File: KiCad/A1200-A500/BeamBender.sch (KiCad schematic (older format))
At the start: 67 parts, among them J1 4-1734742-0, J2 HDMI_A_1.4, J3 STX-3501-3N, J4 Phoenix_Contact, J5 Conn_01x01, U1 LM1117-3.3, U3 ADV7513BSWZ, U4 MCP1702T-1802E_CB, X1 Abracon ASE-27.000MHZ-L-R-T, X2 Oscillator_7.0x5.0mm

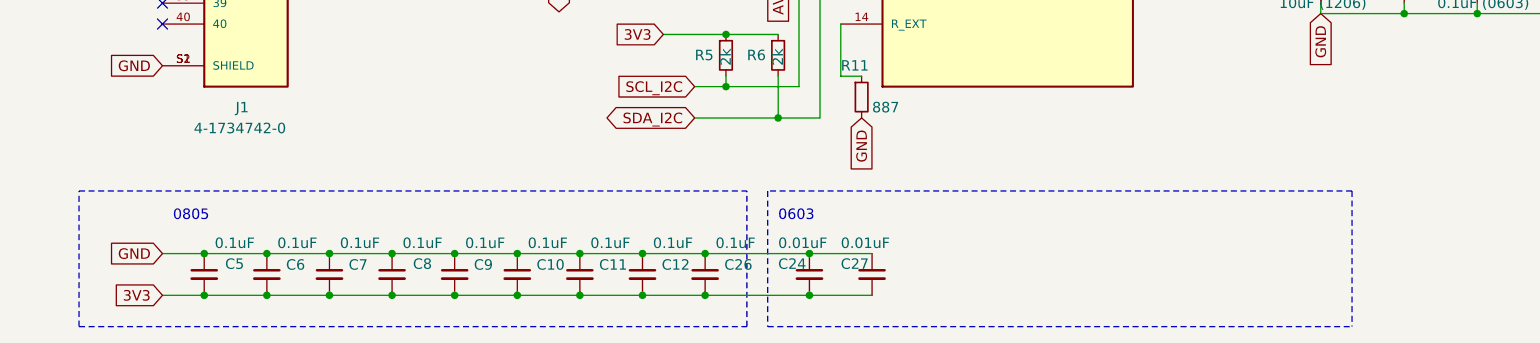
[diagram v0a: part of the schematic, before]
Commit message: Fixed JTAG-connector and remaining 3V3-power routing and pull-ups for FPGA
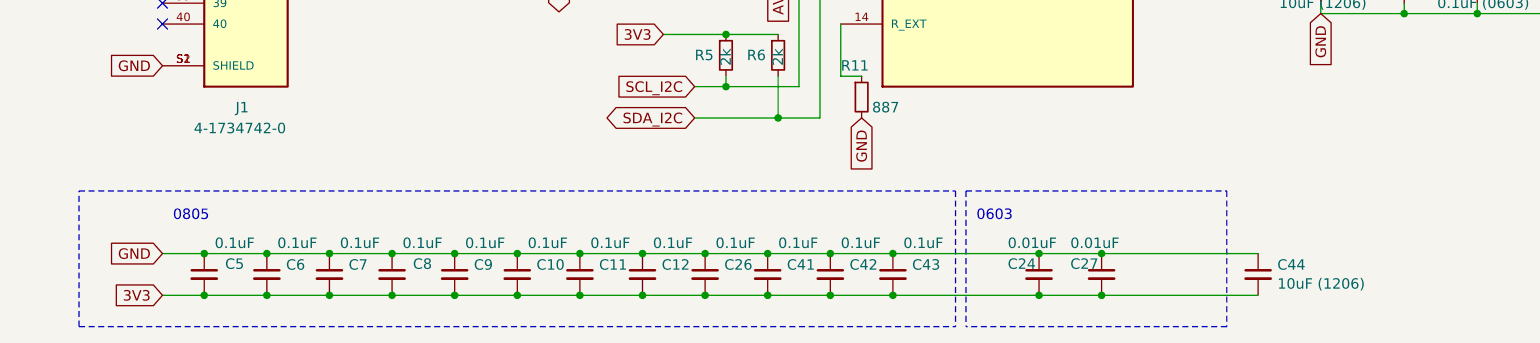
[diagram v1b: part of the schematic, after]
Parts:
- added C41, C42, C43: 0.1uF, Capacitor_SMD:C_0805_2012Metric_Pad1.18x1.45mm_HandSolder, symbol Device:C_Small
- added C44: 10uF (1206), Capacitor_SMD:C_1206_3216Metric_Pad1.33x1.80mm_HandSolder, symbol Device:C_Small
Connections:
- net 3V3: now also C41.2, C42.2, C43.2, C44.2
- net GND: now also C41.1, C42.1, C43.1, C44.1
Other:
- moved on the sheet: C24, C27
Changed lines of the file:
@@
 Connection ~ 2250 7400
 Connection ~ 2250 7600
-Wire Notes Line
-	6850 7100 6850 7750
-Text Notes 4100 7250 0    50   ~ 0
+Text Notes 5050 7250 0    50   ~ 0
 0603
 Wire Wire Line
@@
 L Device:C_Small C24
 U 1 1 6584F5FE
-P 4250 7500
-F 0 "C24" H 4100 7550 50  0000 L CNN
-F 1 "0.01uF" H 4100 7650 50  0000 L CNN
-F 2 "Capacitor_SMD:C_0603_1608Metric_Pad1.08x0.95mm_HandSolder" H 4250 7500 50  0001 C CNN
-F 3 "~" H 4250 7500 50  0001 C CNN
-	1    4250 7500
+P 5350 7500
+F 0 "C24" H 5200 7550 50  0000 L CNN
+F 1 "0.01uF" H 5200 7650 50  0000 L CNN
+F 2 "Capacitor_SMD:C_0603_1608Metric_Pad1.08x0.95mm_HandSolder" H 5350 7500 50  0001 C CNN
+F 3 "~" H 5350 7500 50  0001 C CNN
+	1    5350 7500
 	1    0    0    -1
 $EndComp
@@
 Connection ~ 3450 7400
 Connection ~ 3450 7600
-Wire Notes Line
-	3950 7750 3950 7100
-Wire Notes Line
-	750  7100 3950 7100
-Wire Notes Line
-	750  7750 3950 7750
 Wire Wire Line
 	3450 7400 3750 7400
 Wire Wire Line
 	3450 7600 3750 7600
-Wire Notes Line
-	4050 7100 4050 7750
-Wire Notes Line
-	4050 7750 6850 7750
-Wire Notes Line
-	6850 7100 4050 7100
 $Comp
 L Device:C_Small C26
@@
 $EndComp
 Connection ~ 3750 7400
-Wire Wire Line
-	3750 7400 4250 7400
 Connection ~ 3750 7600
-Wire Wire Line
-	3750 7600 4250 7600
 $Comp
 L Device:C_Small C27
 U 1 1 659B84AB
-P 4550 7500
-F 0 "C27" H 4400 7550 50  0000 L CNN
-F 1 "0.01uF" H 4400 7650 50  0000 L CNN
-F 2 "Capacitor_SMD:C_0603_1608Metric_Pad1.08x0.95mm_HandSolder" H 4550 7500 50  0001 C CNN
-F 3 "~" H 4550 7500 50  0001 C CNN
-	1    4550 7500
-	1    0    0    -1
-$EndComp
-Wire Wire Line
-	4250 7400 4550 7400
-Connection ~ 4250 7400
-Wire Wire Line
-	4250 7600 4550 7600
-Connection ~ 4250 7600
+P 5650 7500
+F 0 "C27" H 5500 7550 50  0000 L CNN
+F 1 "0.01uF" H 5500 7650 50  0000 L CNN
+F 2 "Capacitor_SMD:C_0603_1608Metric_Pad1.08x0.95mm_HandSolder" H 5650 7500 50  0001 C CNN
+F 3 "~" H 5650 7500 50  0001 C CNN
+	1    5650 7500
+	1    0    0    -1
+$EndComp
 $Comp
 L BeamBender:MCP1702T-1802E_CB U4
@@
 Text Notes 6100 3850 0    50   ~ 0
 Drill-hole guide\nfor A500 \n12.5 mm drill
+Wire Wire Line
+	3750 7400 4050 7400
+Wire Wire Line
+	3750 7600 4050 7600
+$Comp
+L Device:C_Small C41
+U 1 1 6639D585
+P 4050 7500
+F 0 "C41" H 4142 7546 50  0000 L CNN
+F 1 "0.1uF" H 4100 7650 50  0000 L CNN
+F 2 "Capacitor_SMD:C_0805_2012Metric_Pad1.18x1.45mm_HandSolder" H 4050 7500 50  0001 C CNN
+F 3 "~" H 4050 7500 50  0001 C CNN
+	1    4050 7500
+	1    0    0    -1
+$EndComp
+Connection ~ 4050 7400
+Wire Wire Line
+	4050 7400 4350 7400
+Connection ~ 4050 7600
+Wire Wire Line
+	4050 7600 4350 7600
+$Comp
+L Device:C_Small C42
+U 1 1 6639DFDF
+P 4350 7500
+F 0 "C42" H 4442 7546 50  0000 L CNN
+F 1 "0.1uF" H 4400 7650 50  0000 L CNN
+F 2 "Capacitor_SMD:C_0805_2012Metric_Pad1.18x1.45mm_HandSolder" H 4350 7500 50  0001 C CNN
+F 3 "~" H 4350 7500 50  0001 C CNN
+	1    4350 7500
+	1    0    0    -1
+$EndComp
+Connection ~ 4350 7400
+Connection ~ 4350 7600
+$Comp
+L Device:C_Small C43
+U 1 1 6639EB03
+P 4650 7500
+F 0 "C43" H 4742 7546 50  0000 L CNN
+F 1 "0.1uF" H 4700 7650 50  0000 L CNN
+F 2 "Capacitor_SMD:C_0805_2012Metric_Pad1.18x1.45mm_HandSolder" H 4650 7500 50  0001 C CNN
+F 3 "~" H 4650 7500 50  0001 C CNN
+	1    4650 7500
+	1    0    0    -1
+$EndComp
+Wire Wire Line
+	4350 7400 4650 7400
+Wire Wire Line
+	4350 7600 4650 7600
+Wire Notes Line
+	5000 7100 5000 7750
+Wire Wire Line
+	4650 7400 5350 7400
+Connection ~ 4650 7400
+Connection ~ 5350 7400
+Wire Wire Line
+	5350 7400 5650 7400
+Wire Wire Line
+	4650 7600 5350 7600
+Connection ~ 4650 7600
+Connection ~ 5350 7600
+Wire Wire Line
+	5350 7600 5650 7600
+Wire Notes Line
+	4950 7100 4950 7750
+Wire Notes Line
+	750  7100 4950 7100
+Wire Notes Line
+	750  7750 4950 7750
+$Comp
+L Device:C_Small C44
+U 1 1 66443446
+P 6400 7500
+F 0 "C44" H 6492 7546 50  0000 L CNN
+F 1 "10uF (1206)" H 6492 7455 50  0000 L CNN
+F 2 "Capacitor_SMD:C_1206_3216Metric_Pad1.33x1.80mm_HandSolder" H 6400 7500 50  0001 C CNN
+F 3 "~" H 6400 7500 50  0001 C CNN
+	1    6400 7500
+	1    0    0    -1
+$EndComp
+Wire Notes Line
+	5000 7100 6250 7100
+Wire Notes Line
+	6250 7100 6250 7750
+Wire Notes Line
+	6250 7750 5000 7750
+Wire Wire Line
+	5650 7400 6400 7400
+Connection ~ 5650 7400
+Wire Wire Line
+	5650 7600 6400 7600
+Connection ~ 5650 7600
 $EndSCHEMATC

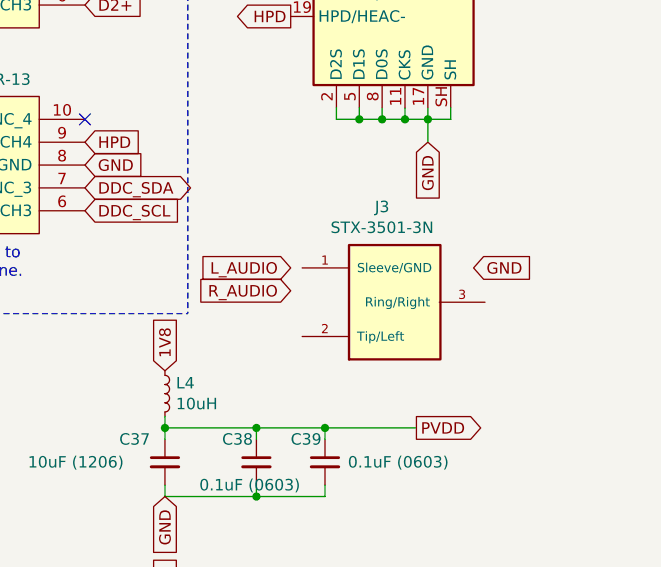
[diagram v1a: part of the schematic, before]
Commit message: assigned the audio Left and Right channels to 3.5mm phono jack (STX-3501-3N) and to ADC-chip (AK5720)
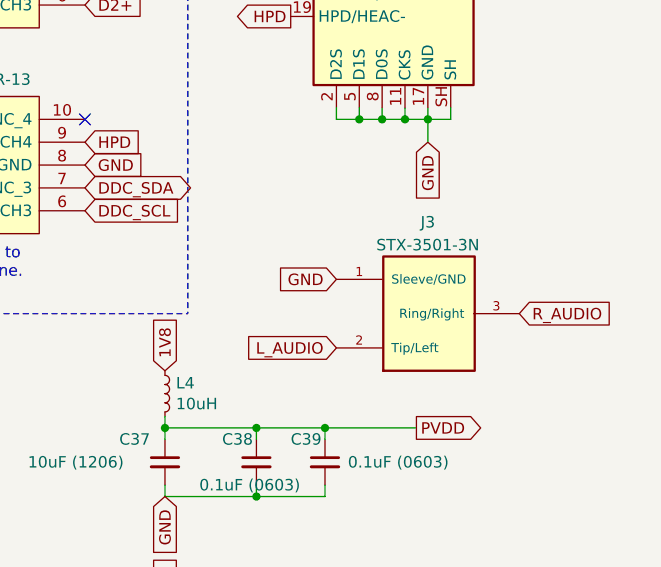
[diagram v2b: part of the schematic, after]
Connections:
- net GND: now also J3.1 (Sleeve/GND)
- net L_AUDIO: now also J3.2 (Tip/Left)
- net R_AUDIO: now also J3.3 (Ring/Right)
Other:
- moved on the sheet: J3
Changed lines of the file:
@@
 L BeamBender:STX-3501-3N J3
 U 1 1 652864E9
-P 10150 4200
-F 0 "J3" H 10100 4517 50  0000 C CNN
-F 1 "STX-3501-3N" H 10100 4426 50  0000 C CNN
-F 2 "BeamBender:STX35013N" H 9950 4850 50  0001 L BNN
-F 3 "" H 9700 4250 50  0001 L BNN
-	1    10150 4200
+P 10300 4250
+F 0 "J3" H 10300 4550 50  0000 C CNN
+F 1 "STX-3501-3N" H 10300 4450 50  0000 C CNN
+F 2 "BeamBender:STX35013N" H 10100 4900 50  0001 L BNN
+F 3 "" H 9850 4300 50  0001 L BNN
+	1    10300 4250
 	1    0    0    -1
 $EndComp
-Text GLabel 10500 4150 2    50   Input ~ 0
+Text GLabel 9900 4200 0    50   Input ~ 0
 GND
-Text GLabel 9700 4150 0    50   Input ~ 0
+Text GLabel 9900 4500 0    50   Input ~ 0
 L_AUDIO
-Text GLabel 9700 4250 0    50   Input ~ 0
+Text GLabel 10700 4350 2    50   Input ~ 0
 R_AUDIO
 Text GLabel 6000 5100 3    50   Input ~ 0

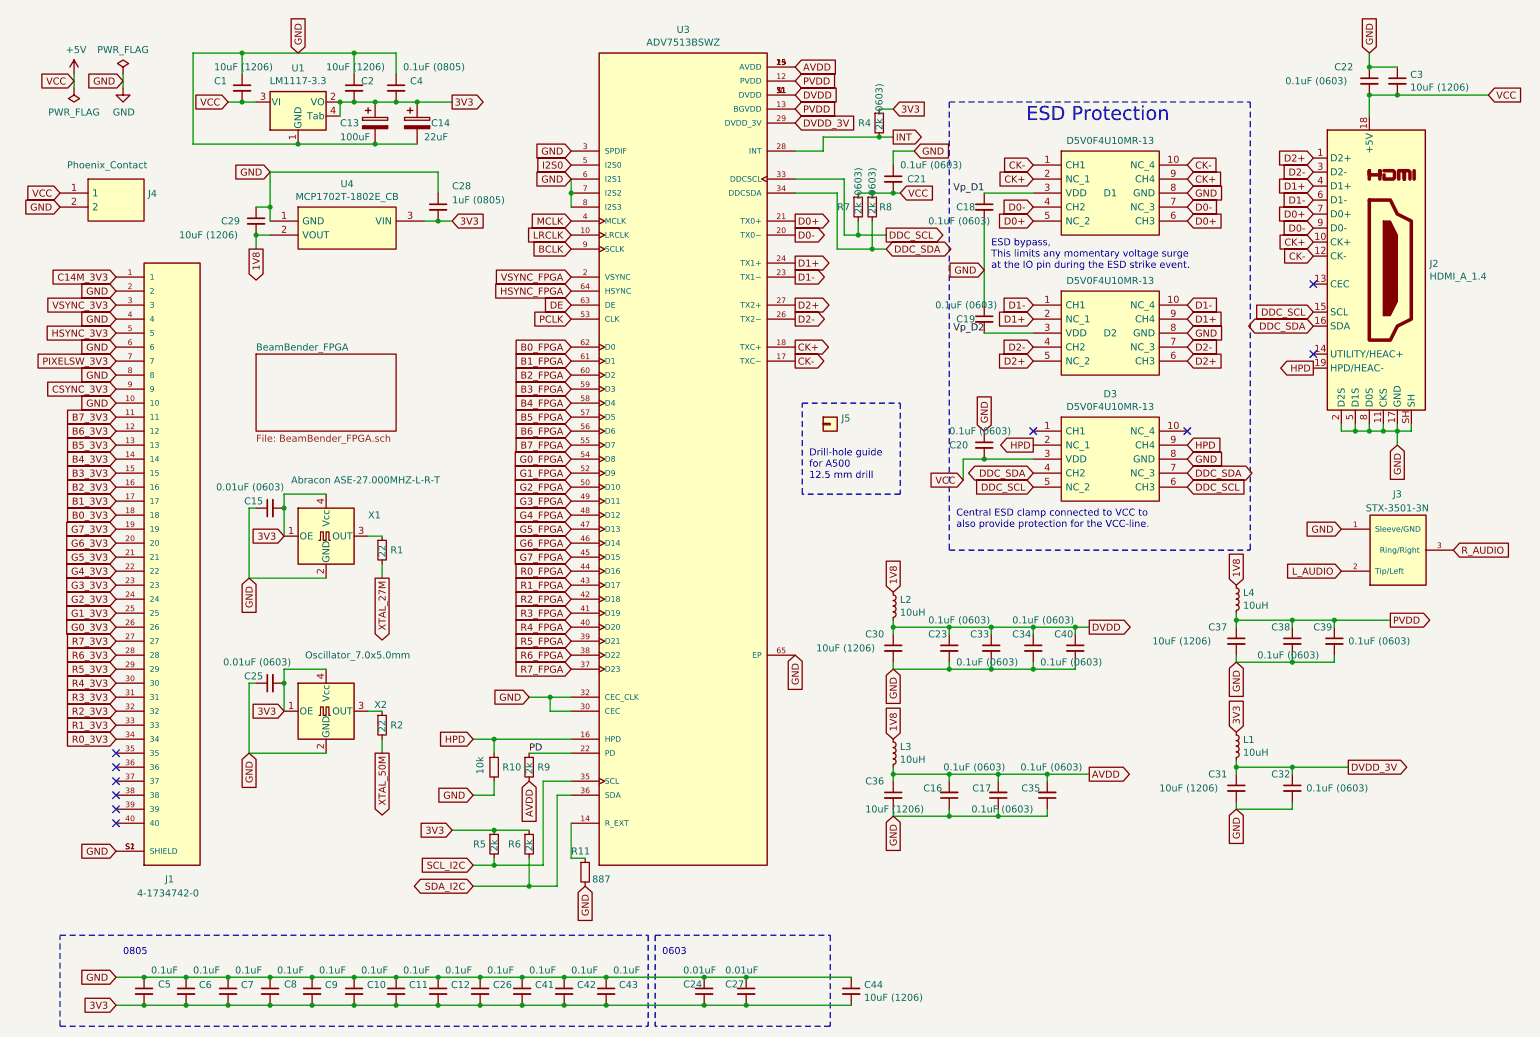
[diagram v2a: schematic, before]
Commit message: Fixed assignment/enumeration of all capacitors from C1 to C54
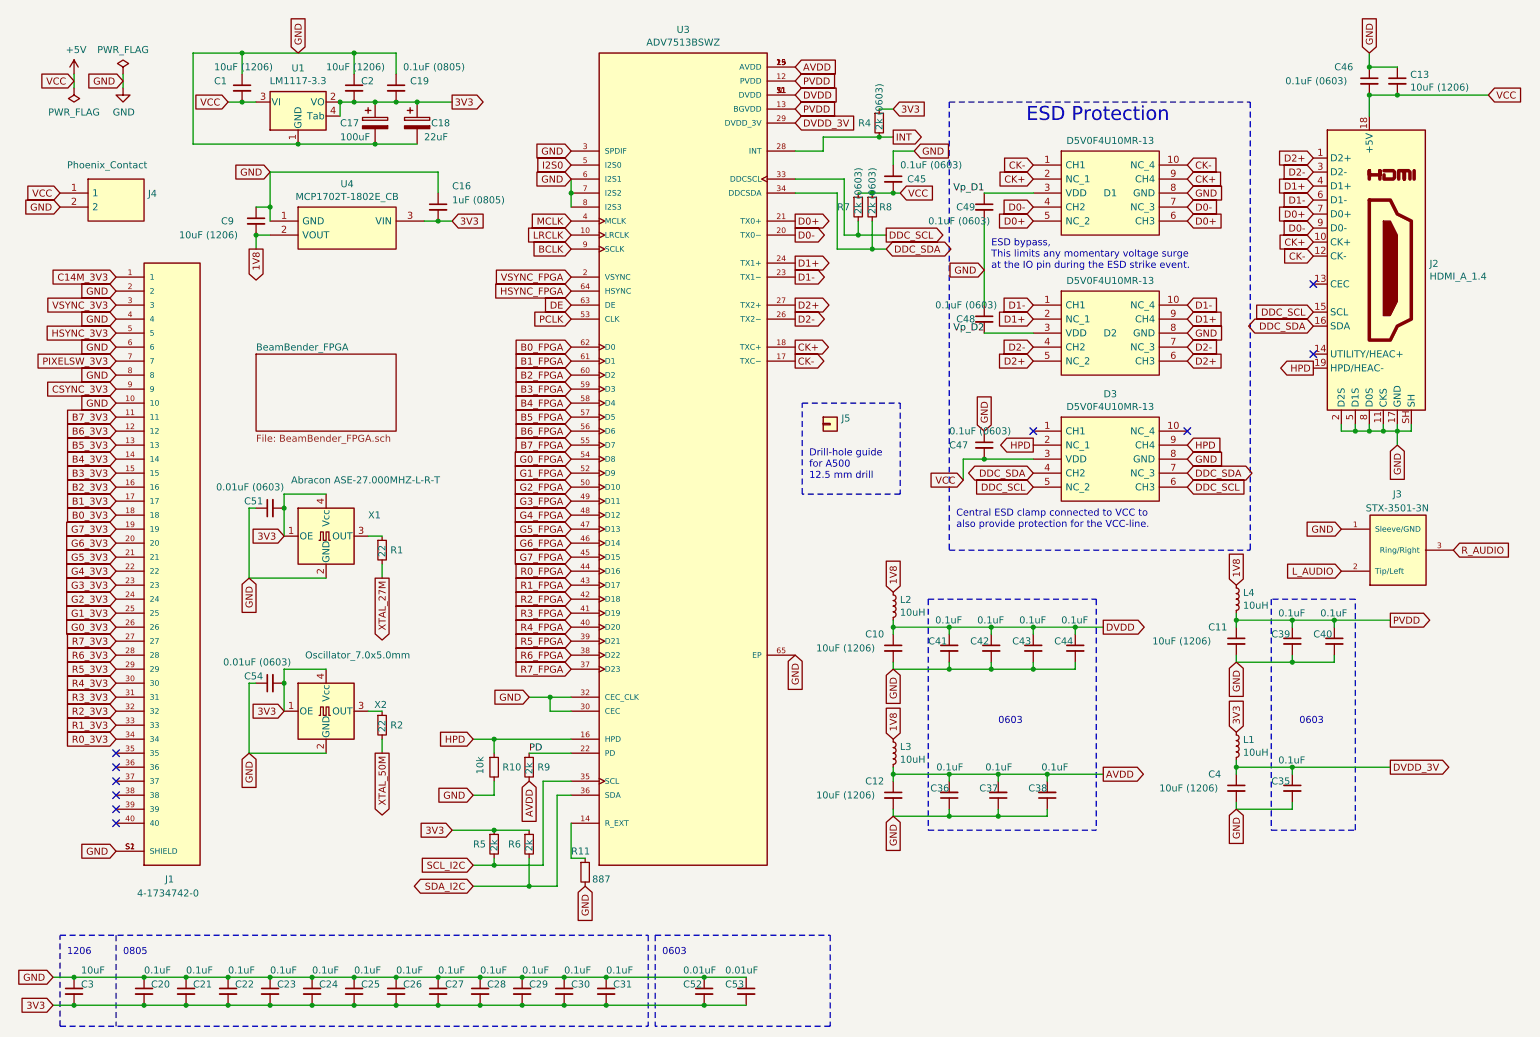
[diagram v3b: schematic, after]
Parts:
- C3: renamed from C44; value 10uF (1206) -> 10uF
- C35: renamed from C32; value 0.1uF (0603) -> 0.1uF
- C36: renamed from C16; value 0.1uF (0603) -> 0.1uF
- C37: renamed from C17; value 0.1uF (0603) -> 0.1uF
- C38: renamed from C35; value 0.1uF (0603) -> 0.1uF
- C39: renamed from C38; value 0.1uF (0603) -> 0.1uF
- C40: renamed from C39; value 0.1uF (0603) -> 0.1uF
- C41: renamed from C40; value 0.1uF (0603) -> 0.1uF
- C42: renamed from C34; value 0.1uF (0603) -> 0.1uF
- C43: renamed from C23; value 0.1uF (0603) -> 0.1uF
- C44: renamed from C33; value 0.1uF (0603) -> 0.1uF
- renumbered C30 to C10, C37 to C11, C36 to C12, C3 to C13, C28 to C16, C13 to C17, C14 to C18, C4 to C19, C5 to C20, C6 to C21, C7 to C22, C8 to C23, C11 to C24, C9 to C25, C43 to C27, C42 to C28, C41 to C29, C10 to C30, C12 to C31, C31 to C4, C21 to C45, C22 to C46, C20 to C47, C19 to C48, C18 to C49, C15 to C51, C27 to C52, C24 to C53, C25 to C54, C29 to C9
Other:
- note added: "1206"
- moved on the sheet: C24, C25, C26, C27, C28, C3, C30, C31, C41, C42, C43, C44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

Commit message: Fixed enumeration/order of all resistors on board and their reference placement on silkscreen
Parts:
- renumbered R4 to R10, R6 to R11, R9 to R12, R11 to R13, R2 to R14, R1 to R15, R10 to R22, R5 to R9
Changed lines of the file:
@@
 XTAL_27M
 $Comp
-L Device:R_Small R1
+L Device:R_Small R15
 U 1 1 65512C64
 P 3050 4350
-F 0 "R1" H 3109 4350 50  0000 L CNN
+F 0 "R15" H 3109 4350 50  0000 L CNN
 F 1 "22" V 3050 4300 50  0000 L CNN
 F 2 "Resistor_SMD:R_0603_1608Metric_Pad0.98x0.95mm_HandSolder" H 3050 4350 50  0001 C CNN
@@
 	4100 5800 4400 5800
 $Comp
-L Device:R_Small R9
+L Device:R_Small R12
 U 1 1 6531102F
 P 4100 5900
-F 0 "R9" H 4159 5900 50  0000 L CNN
+F 0 "R12" H 4159 5900 50  0000 L CNN
 F 1 "2k" V 4100 5850 50  0000 L CNN
 F 2 "Resistor_SMD:R_0603_1608Metric_Pad0.98x0.95mm_HandSolder" H 4100 5900 50  0001 C CNN
@@
 Text GLabel 3700 6100 0    50   Input ~ 0
 GND
-$Comp
-L Device:R_Small R10
-U 1 1 652DC9C5
-P 3850 5900
-F 0 "R10" H 3909 5900 50  0000 L CNN
-F 1 "10k" V 3750 5850 50  0000 L CNN
-F 2 "Resistor_SMD:R_0603_1608Metric_Pad0.98x0.95mm_HandSolder" H 3850 5900 50  0001 C CNN
-F 3 "~" H 3850 5900 50  0001 C CNN
-	1    3850 5900
-	1    0    0    -1
-$EndComp
 Text GLabel 3700 5700 0    50   Input ~ 0
 HPD
@@
 Wire Wire Line
 	4300 6100 4400 6100
-$Comp
-L Device:R_Small R5
-U 1 1 655C6F45
-P 3850 6450
-F 0 "R5" H 3700 6450 50  0000 L CNN
-F 1 "2k" V 3850 6400 50  0000 L CNN
-F 2 "Resistor_SMD:R_0603_1608Metric_Pad0.98x0.95mm_HandSolder" H 3850 6450 50  0001 C CNN
-F 3 "~" H 3850 6450 50  0001 C CNN
-	1    3850 6450
-	1    0    0    -1
-$EndComp
 Text GLabel 3550 6350 0    50   Input ~ 0
 3V3
@@
 Wire Wire Line
 	3850 6600 4200 6600
-$Comp
-L Device:R_Small R6
-U 1 1 655D3232
-P 4100 6450
-F 0 "R6" H 3950 6450 50  0000 L CNN
-F 1 "2k" V 4100 6400 50  0000 L CNN
-F 2 "Resistor_SMD:R_0603_1608Metric_Pad0.98x0.95mm_HandSolder" H 4100 6450 50  0001 C CNN
-F 3 "~" H 4100 6450 50  0001 C CNN
-	1    4100 6450
-	1    0    0    -1
-$EndComp
 Wire Wire Line
 	3850 6350 4100 6350
@@
 Text GLabel 4400 2700 0    50   Input ~ 0
 PCLK
-$Comp
-L Device:R_Small R4
-U 1 1 656847D2
-P 6600 1300
-F 0 "R4" H 6450 1300 50  0000 L CNN
-F 1 "2k  (0603)" V 6600 1250 50  0000 L CNN
-F 2 "Resistor_SMD:R_0603_1608Metric_Pad0.98x0.95mm_HandSolder" H 6600 1300 50  0001 C CNN
-F 3 "~" H 6600 1300 50  0001 C CNN
-	1    6600 1300
-	1    0    0    -1
-$EndComp
 Wire Wire Line
 	6450 2100 6350 2100
@@
 	2350 5200 2350 5300
 $Comp
-L Device:R_Small R2
+L Device:R_Small R14
 U 1 1 6589F17E
 P 3050 5600
-F 0 "R2" H 3109 5600 50  0000 L CNN
+F 0 "R14" H 3109 5600 50  0000 L CNN
 F 1 "22" V 3050 5550 50  0000 L CNN
 F 2 "Resistor_SMD:R_0603_1608Metric_Pad0.98x0.95mm_HandSolder" H 3050 5600 50  0001 C CNN
@@
 	7700 5200 7400 5200
 Connection ~ 7400 5200
-$Comp
-L Device:R_Small R11
-U 1 1 65DD51EC
-P 4500 6650
-F 0 "R11" H 4400 6800 50  0000 L CNN
-F 1 "887" H 4550 6600 50  0000 L CNN
-F 2 "Resistor_SMD:R_0603_1608Metric_Pad0.98x0.95mm_HandSolder" H 4500 6650 50  0001 C CNN
-F 3 "~" H 4500 6650 50  0001 C CNN
-	1    4500 6650
-	1    0    0    -1
-$EndComp
 Wire Wire Line
 	4400 6300 4400 6550
@@
 Text Notes 9600 5600 0    50   ~ 0
 0603
+$Comp
+L Device:R_Small R10
+U 1 1 656847D2
+P 6600 1300
+F 0 "R10" H 6400 1300 50  0000 L CNN
+F 1 "2k  (0603)" V 6600 1250 50  0000 L CNN
+F 2 "Resistor_SMD:R_0603_1608Metric_Pad0.98x0.95mm_HandSolder" H 6600 1300 50  0001 C CNN
+F 3 "~" H 6600 1300 50  0001 C CNN
+	1    6600 1300
+	1    0    0    -1
+$EndComp
+$Comp
+L Device:R_Small R13
+U 1 1 65DD51EC
+P 4500 6650
+F 0 "R13" H 4400 6800 50  0000 L CNN
+F 1 "887" H 4550 6600 50  0000 L CNN
+F 2 "Resistor_SMD:R_0603_1608Metric_Pad0.98x0.95mm_HandSolder" H 4500 6650 50  0001 C CNN
+F 3 "~" H 4500 6650 50  0001 C CNN
+	1    4500 6650
+	1    0    0    -1
+$EndComp
+$Comp
+L Device:R_Small R22
+U 1 1 652DC9C5
+P 3850 5900
+F 0 "R22" H 3909 5900 50  0000 L CNN
+F 1 "10k" V 3750 5850 50  0000 L CNN
+F 2 "Resistor_SMD:R_0603_1608Metric_Pad0.98x0.95mm_HandSolder" H 3850 5900 50  0001 C CNN
+F 3 "~" H 3850 5900 50  0001 C CNN
+	1    3850 5900
+	1    0    0    -1
+$EndComp
+$Comp
+L Device:R_Small R11
+U 1 1 655D3232
+P 4100 6450
+F 0 "R11" H 3900 6450 50  0000 L CNN
+F 1 "2k" V 4100 6400 50  0000 L CNN
+F 2 "Resistor_SMD:R_0603_1608Metric_Pad0.98x0.95mm_HandSolder" H 4100 6450 50  0001 C CNN
+F 3 "~" H 4100 6450 50  0001 C CNN
+	1    4100 6450
+	1    0    0    -1
+$EndComp
+$Comp
+L Device:R_Small R9
+U 1 1 655C6F45
+P 3850 6450
+F 0 "R9" H 3700 6450 50  0000 L CNN
+F 1 "2k" V 3850 6400 50  0000 L CNN
+F 2 "Resistor_SMD:R_0603_1608Metric_Pad0.98x0.95mm_HandSolder" H 3850 6450 50  0001 C CNN
+F 3 "~" H 3850 6450 50  0001 C CNN
+	1    3850 6450
+	1    0    0    -1
+$EndComp
 $EndSCHEMATC
